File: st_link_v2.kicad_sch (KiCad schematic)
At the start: 22 parts, among them SW401 STLINK_RST, U401 STM32F103CBTx, Y401 8MHz 5pF

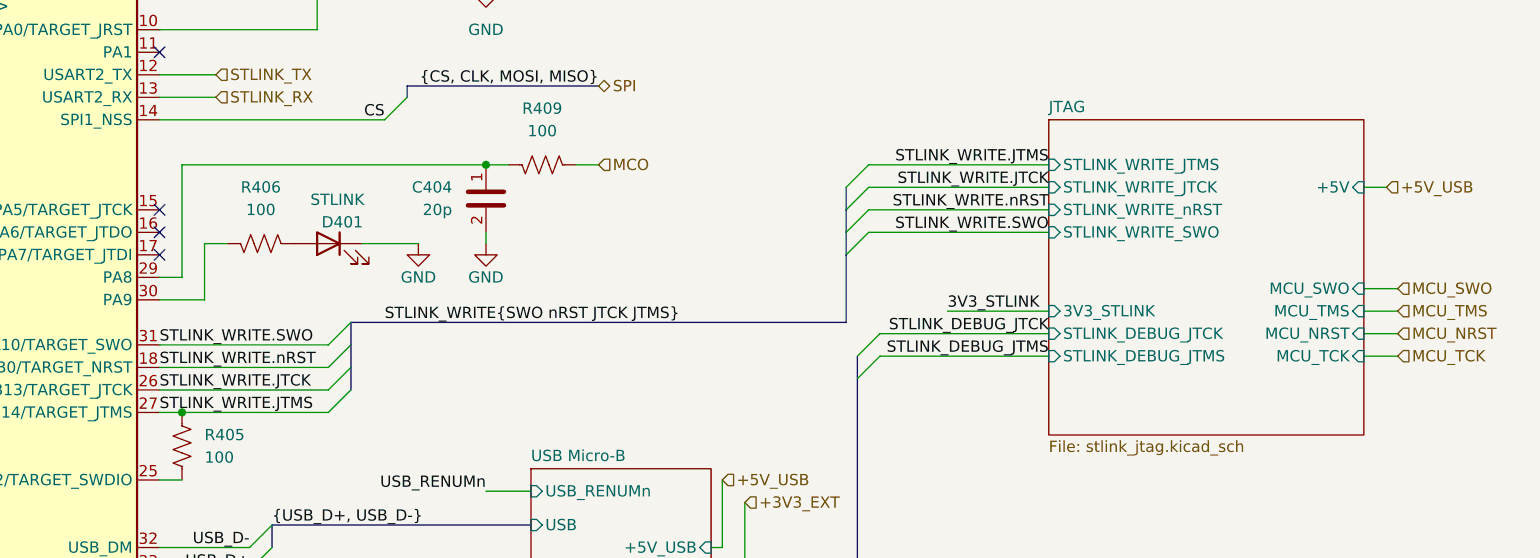
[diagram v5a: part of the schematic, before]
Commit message: small schematic changes, need to reroute
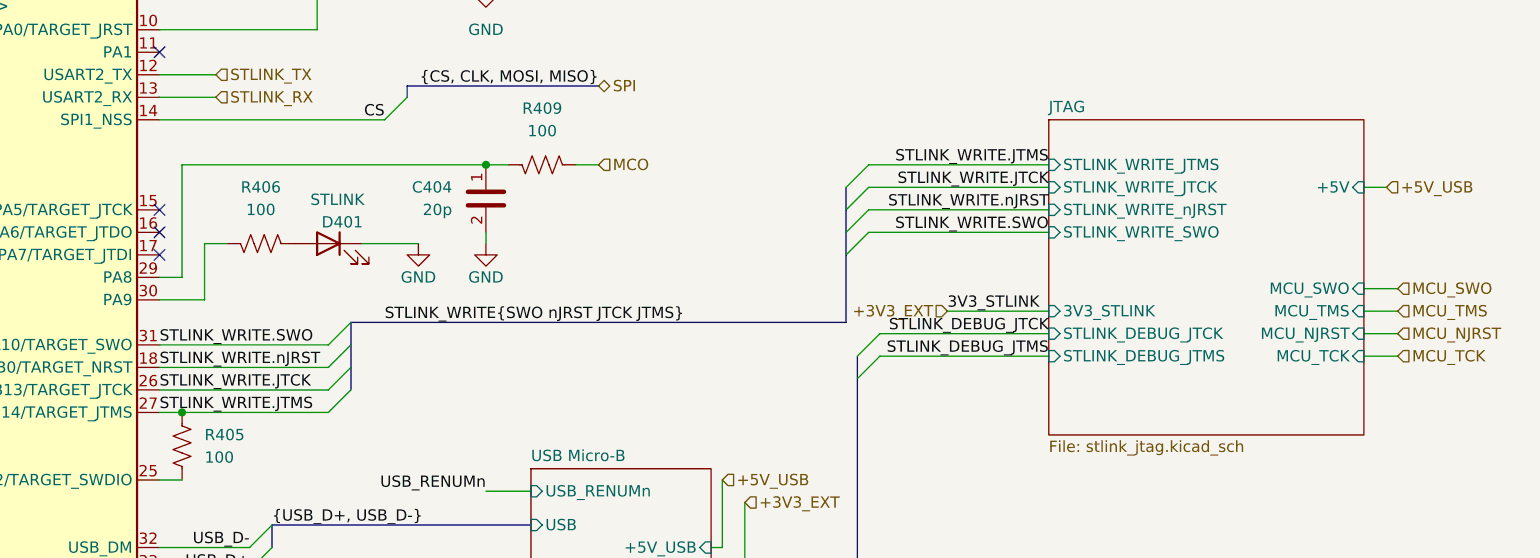
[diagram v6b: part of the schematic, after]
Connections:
- net STLINK_WRITE.nRST renamed STLINK_WRITE.nJRST
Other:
- sheet JTAG ports: added MCU_NJRST, STLINK_WRITE_nJRST; removed MCU_NRST, STLINK_WRITE_nRST
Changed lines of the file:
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@@
 		)
 	)
-	(label "STLINK_WRITE.nRST"
+	(label "STLINK_WRITE.nJRST"
 		(at 234.95 80.01 180)
 		(effects
@@
 		)
 	)
-	(label "STLINK_WRITE{SWO nRST JTCK JTMS}"
+	(label "STLINK_WRITE{SWO nJRST JTCK JTMS}"
 		(at 160.02 92.71 0)
 		(effects
@@
 		)
 	)
-	(label "STLINK_WRITE.nRST"
+	(label "STLINK_WRITE.nJRST"
 		(at 134.62 97.79 0)
 		(effects
@@
 		)
 	)
+	(hierarchical_label "+3V3_EXT"
+		(shape input)
+		(at 223.52 91.44 180)
+		(effects
+			(font
+				(size 1.27 1.27)
+			)
+			(justify right)
+		)
+	)
 	(hierarchical_label "MCO"
 		(shape input)
@@
 		)
 	)
-	(hierarchical_label "MCU_NRST"
+	(hierarchical_label "MCU_NJRST"
 		(shape input)
 		(at 274.32 93.98 0)
@@
 			)
 		)
-		(pin "STLINK_WRITE_nRST" input
+		(pin "STLINK_WRITE_nJRST" input
 			(at 234.95 80.01 180)
 			(effects
@@
 			)
 		)
-		(pin "MCU_NRST" input
+		(pin "MCU_NJRST" input
 			(at 270.51 93.98 0)
 			(effects
